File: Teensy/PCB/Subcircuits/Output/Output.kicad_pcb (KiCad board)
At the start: 2 copper layers, 5 parts

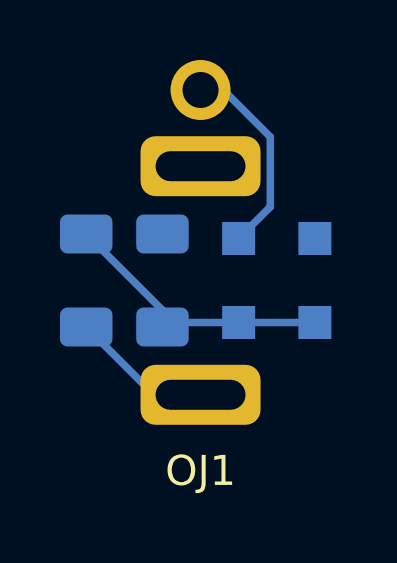
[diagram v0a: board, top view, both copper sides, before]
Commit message: Added Panel PCBs
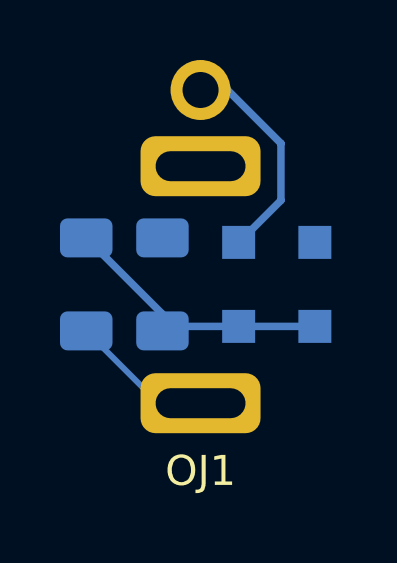
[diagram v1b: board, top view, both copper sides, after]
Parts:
- moved OD1 0.13 mm to (97.8, 90.3)
- moved OD2 0.13 mm to (100.3, 90.3)
- moved OR1 0.13 mm to (92.7, 90.3)
- moved OR2 0.13 mm to (95.2, 90.3)
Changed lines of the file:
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@@
   )
   (setup
+    (stackup
+      (layer "F.SilkS" (type "Top Silk Screen"))
+      (layer "F.Paste" (type "Top Solder Paste"))
+      (layer "F.Mask" (type "Top Solder Mask") (thickness 0.01))
+      (layer "F.Cu" (type "copper") (thickness 0.035))
+      (layer "dielectric 1" (type "core") (thickness 1.51) (material "FR4") (epsilon_r 4.5) (loss_tangent 0.02))
+      (layer "B.Cu" (type "copper") (thickness 0.035))
+      (layer "B.Mask" (type "Bottom Solder Mask") (thickness 0.01))
+      (layer "B.Paste" (type "Bottom Solder Paste"))
+      (layer "B.SilkS" (type "Bottom Silk Screen"))
+      (copper_finish "None")
+      (dielectric_constraints no)
+    )
     (pad_to_mask_clearance 0)
     (pcbplotparams
@@
   (footprint "Perfboard:3.5mm Jack Perfboard" (layer "F.Cu")
     (at 96.52 88.9)
-    (property "Sheetfile" "../Subcircuits/Output/Output.kicad_sch")
-    (property "Sheetname" "Output")
+    (property "Sheetfile" "Output.kicad_sch")
+    (property "Sheetname" "")
     (attr through_hole)
     (fp_text reference "OJ1" (at 0 7.62 unlocked) (layer "F.SilkS")
@@
       (effects (font (size 1 1) (thickness 0.15)))
     )
-    (fp_line (start -2.54 -3.81) (end -3.81 -3.81) (layer "Dwgs.User") (width 0.12))
-    (fp_line (start 2.54 -3.81) (end 3.81 -3.81) (layer "Dwgs.User") (width 0.12))
-    (fp_line (start -3.81 -3.81) (end -3.81 6.35) (layer "Dwgs.User") (width 0.12))
-    (fp_line (start -2.54 6.35) (end 2.54 6.35) (layer "Dwgs.User") (width 0.12))
-    (fp_line (start -3.81 6.35) (end -2.54 6.35) (layer "Dwgs.User") (width 0.12))
-    (fp_line (start 3.81 6.35) (end 2.54 6.35) (layer "Dwgs.User") (width 0.12))
-    (fp_line (start 2.54 -3.81) (end -2.54 -3.81) (layer "Dwgs.User") (width 0.12))
-    (fp_line (start 3.81 -3.81) (end 3.81 6.35) (layer "Dwgs.User") (width 0.12))
-    (fp_circle (center 0 0.83) (end 3.25 0.83) (layer "User.2") (width 0.12) (fill none))
+    (fp_rect (start -3.8 -3.94) (end 3.8 6.56) (layer "F.CrtYd") (width 0.12) (fill none))
+    (fp_circle (center 0 0.86) (end 3.25 0.86) (layer "User.2") (width 0.12) (fill none))
     (pad "G" thru_hole circle (at 0 -5.08) (size 2 2) (drill 1.2) (layers *.Cu *.Mask)
       (pintype "passive"))
     (pad "S" thru_hole roundrect (at 0 -2.54) (size 4 2) (drill oval 3 1) (layers *.Cu *.Mask) (roundrect_rratio 0.25)
       (pintype "passive"))
-    (pad "T" thru_hole roundrect (at 0 5.08) (size 4 2) (drill oval 3 1) (layers *.Cu *.Mask) (roundrect_rratio 0.25)
+    (pad "T" thru_hole roundrect (at 0 5.36) (size 4 2) (drill oval 3 1) (layers *.Cu *.Mask) (roundrect_rratio 0.25)
       (pintype "passive"))
     (model "C:/Users/Florian/Documents/KiCad/6.0/3dmodels/PTV09/PJ301M-12 Thonkiconn v0.2.stp"
-      (offset (xyz 0 -1 0))
+      (offset (xyz 0 -1.5 0))
       (scale (xyz 1 1 1))
       (rotate (xyz 0 0 180))
@@
   )
   (footprint "Diode_SMD:D_SOD-123F" (layer "B.Cu")
-    (at 100.33 90.17 -90)
+    (at 100.33 90.3 -90)
     (descr "D_SOD-123F")
     (tags "D_SOD-123F")
-    (property "Sheetfile" "../Subcircuits/Output/Output.kicad_sch")
-    (property "Sheetname" "Output")
-    (attr smd)
-    (fp_text reference "OD2" (at -0.127 1.905 90) (layer "B.SilkS")
-      (effects (font (size 1 1) (thickness 0.15)) (justify mirror))
-    )
-    (fp_text value "240mV" (at 0 -2.1 90) (layer "B.Fab")
-      (effects (font (size 1 1) (thickness 0.15)) (justify mirror))
-    )
-    (fp_text user "${REFERENCE}" (at -0.127 1.905 90) (layer "B.Fab")
+    (property "Sheetfile" "Output.kicad_sch")
+    (property "Sheetname" "")
+    (attr smd)
+    (fp_text reference "OD2" (at -0.127 1.905 90) (layer "B.SilkS") hide
+      (effects (font (size 1 1) (thickness 0.15)) (justify mirror))
+    )
+    (fp_text value "240mV" (at 0 -2.1 90) (layer "B.SilkS")
+      (effects (font (size 1 1) (thickness 0.15)) (justify mirror))
+    )
+    (fp_text user "${REFERENCE}" (at -0.127 1.905 90) (layer "B.Fab") hide
       (effects (font (size 1 1) (thickness 0.15)) (justify mirror))
     )
@@
   )
   (footprint "Diode_SMD:D_SOD-123F" (layer "B.Cu")
-    (at 97.79 90.17 90)
+    (at 97.79 90.3 90)
     (descr "D_SOD-123F")
     (tags "D_SOD-123F")
-    (property "Sheetfile" "../Subcircuits/Output/Output.kicad_sch")
-    (property "Sheetname" "Output")
-    (attr smd)
-    (fp_text reference "OD1" (at -0.127 1.905 90) (layer "B.SilkS")
-      (effects (font (size 1 1) (thickness 0.15)) (justify mirror))
-    )
-    (fp_text value "240mV" (at 0 -2.1 90) (layer "B.Fab")
-      (effects (font (size 1 1) (thickness 0.15)) (justify mirror))
-    )
-    (fp_text user "${REFERENCE}" (at -0.127 1.905 90) (layer "B.Fab")
+    (property "Sheetfile" "Output.kicad_sch")
+    (property "Sheetname" "")
+    (attr smd)
+    (fp_text reference "OD1" (at -0.127 1.905 90) (layer "B.SilkS") hide
+      (effects (font (size 1 1) (thickness 0.15)) (justify mirror))
+    )
+    (fp_text value "240mV" (at 0 -2.1 90) (layer "B.Fab") hide
+      (effects (font (size 1 1) (thickness 0.15)) (justify mirror))
+    )
+    (fp_text user "${REFERENCE}" (at -3.302 3.302 90) (layer "B.Fab") hide
       (effects (font (size 1 1) (thickness 0.15)) (justify mirror))
     )
@@
   )
   (footprint "Resistor_SMD:R_1206_3216Metric_Pad1.30x1.75mm_HandSolder" (layer "B.Cu")
-    (at 95.25 90.17 90)
+    (at 95.25 90.3 90)
     (descr "Resistor SMD 1206 (3216 Metric), square (rectangular) end terminal, IPC_7351 nominal with elongated pad for handsoldering. (Body size source: IPC-SM-782 page 72, https://www.pcb-3d.com/wordpress/wp-content/uploads/ipc-sm-782a_amendment_1_and_2.pdf), generated with kicad-footprint-generator")
     (tags "resistor handsolder")
-    (property "Sheetfile" "../Subcircuits/Output/Output.kicad_sch")
-    (property "Sheetname" "Output")
-    (attr smd)
-    (fp_text reference "OR2" (at 0 1.82 90) (layer "B.SilkS")
-      (effects (font (size 1 1) (thickness 0.15)) (justify mirror))
-    )
-    (fp_text value "900" (at 0 -1.82 90) (layer "B.Fab")
+    (property "Sheetfile" "Output.kicad_sch")
+    (property "Sheetname" "")
+    (attr smd)
+    (fp_text reference "OR2" (at 0 1.82 90) (layer "B.SilkS") hide
+      (effects (font (size 1 1) (thickness 0.15)) (justify mirror))
+    )
+    (fp_text value "900" (at -4.064 -1.778 90) (layer "B.SilkS") hide
       (effects (font (size 1 1) (thickness 0.15)) (justify mirror))
     )
@@
   )
   (footprint "Resistor_SMD:R_1206_3216Metric_Pad1.30x1.75mm_HandSolder" (layer "B.Cu")
-    (at 92.71 90.17 90)
+    (at 92.71 90.3 90)
     (descr "Resistor SMD 1206 (3216 Metric), square (rectangular) end terminal, IPC_7351 nominal with elongated pad for handsoldering. (Body size source: IPC-SM-782 page 72, https://www.pcb-3d.com/wordpress/wp-content/uploads/ipc-sm-782a_amendment_1_and_2.pdf), generated with kicad-footprint-generator")
     (tags "resistor handsolder")
-    (property "Sheetfile" "../Subcircuits/Output/Output.kicad_sch")
-    (property "Sheetname" "Output")
-    (attr smd)
-    (fp_text reference "OR1" (at 0 1.82 90) (layer "B.SilkS")
-      (effects (font (size 1 1) (thickness 0.15)) (justify mirror))
-    )
-    (fp_text value "100" (at 0 -1.82 90) (layer "B.Fab")
+    (property "Sheetfile" "Output.kicad_sch")
+    (property "Sheetname" "")
+    (attr smd)
+    (fp_text reference "OR1" (at 0 1.82 90) (layer "B.SilkS") hide
+      (effects (font (size 1 1) (thickness 0.15)) (justify mirror))
+    )
+    (fp_text value "100" (at 0 -1.82 90) (layer "B.SilkS")
       (effects (font (size 1 1) (thickness 0.15)) (justify mirror))
     )
@@
     )
   )
-  (segment (start 98.845 87.715) (end 98.845 85.383) (width 0.25) (layer "B.Cu") (net 0))
-  (segment (start 98.845 85.383) (end 97.282 83.82) (width 0.25) (layer "B.Cu") (net 0))
-  (segment (start 97.79 88.77) (end 98.845 87.715) (width 0.25) (layer "B.Cu") (net 0))
-  (segment (start 95.25 88.62) (end 94.97 88.62) (width 0.25) (layer "B.Cu") (net 0))
-  (segment (start 95.4 91.57) (end 97.79 91.57) (width 0.25) (layer "B.Cu") (net 0))
-  (segment (start 95.25 91.72) (end 95.4 91.57) (width 0.25) (layer "B.Cu") (net 0))
-  (segment (start 92.71 88.62) (end 95.25 91.16) (width 0.25) (layer "B.Cu") (net 0))
-  (segment (start 94.97 93.98) (end 92.71 91.72) (width 0.25) (layer "B.Cu") (net 0))
-  (segment (start 97.282 83.82) (end 96.52 83.82) (width 0.25) (layer "B.Cu") (net 0))
-  (segment (start 96.52 93.98) (end 94.97 93.98) (width 0.25) (layer "B.Cu") (net 0))
-  (segment (start 95.25 91.16) (end 95.25 91.72) (width 0.25) (layer "B.Cu") (net 0))
-  (segment (start 97.79 91.57) (end 100.33 91.57) (width 0.25) (layer "B.Cu") (net 0))
+  (segment (start 99.2 87.5) (end 99.2 85.6) (width 0.25) (layer "B.Cu") (net 0))
+  (segment (start 97.42 83.82) (end 96.52 83.82) (width 0.25) (layer "B.Cu") (net 0))
+  (segment (start 92.71 91.85) (end 95.12 94.26) (width 0.2) (layer "B.Cu") (net 0))
+  (segment (start 95.4 91.7) (end 97.79 91.7) (width 0.25) (layer "B.Cu") (net 0))
+  (segment (start 95.25 91.85) (end 95.4 91.7) (width 0.25) (layer "B.Cu") (net 0))
+  (segment (start 97.79 88.9) (end 97.8 88.9) (width 0.25) (layer "B.Cu") (net 0))
+  (segment (start 95.12 94.26) (end 96.52 94.26) (width 0.2) (layer "B.Cu") (net 0))
+  (segment (start 92.71 88.75) (end 95.25 91.29) (width 0.25) (layer "B.Cu") (net 0))
+  (segment (start 99.2 85.6) (end 97.42 83.82) (width 0.25) (layer "B.Cu") (net 0))
+  (segment (start 95.25 91.29) (end 95.25 91.85) (width 0.25) (layer "B.Cu") (net 0))
+  (segment (start 97.8 88.9) (end 99.2 87.5) (width 0.25) (layer "B.Cu") (net 0))
+  (segment (start 97.79 91.7) (end 100.33 91.7) (width 0.25) (layer "B.Cu") (net 0))
 )

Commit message: Made NPTH holes 0.5mm bigger; adjusted diode pads for better solderability
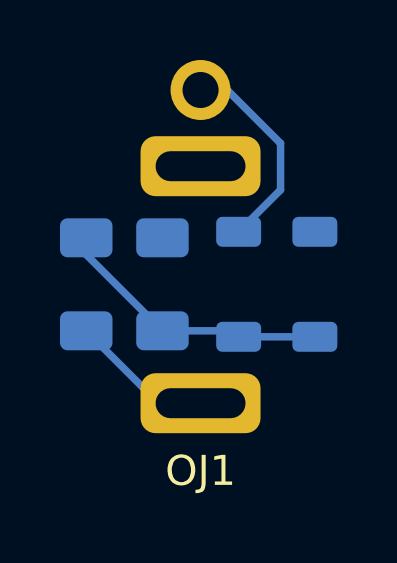
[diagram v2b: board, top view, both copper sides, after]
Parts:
- OD1, OD2: footprint Diode_SMD:D_SOD-123F -> Misc:D_SOD-123 Handsolder
